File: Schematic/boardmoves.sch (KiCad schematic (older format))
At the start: 27 parts, among them U1 74LS107, U2 74LS107, U3 74LS107, U4 74LS107, U5 74LS107, U6 74LS107, U7 74LS107, U8 74LS107, U9 74LS107

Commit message: More work on the circuit and the PCB layout.
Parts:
- R28, R29, R30, R31, R32, R33, R34, R35, R36: value 10K -> 1K
- U1, U2, U3, U4, U5, U6, U7, U8, U9: value 74LS107 -> 74LS109
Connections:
- wire segments 81 -> 90
- no-connect marks 18 -> 9
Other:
- moved on the sheet: D10, D11, D12, D13, D14, D15, D16, D17, D18, R28, R29, R30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

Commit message: Updated the schematic and PCB with the new flip-flip pinouts and footprints.
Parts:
- U1, U2, U3, U4, U5, U6, U7, U8, U9: footprint Package_DIP:DIP-14_W7.62mm -> Package_DIP:DIP-16_W7.62mm; symbol ttt_ttl-rescue:74LS107 -> local:74LS107
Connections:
- net labels added: Hi
- wire segments 90 -> 108
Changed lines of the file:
@@
 	1200 1600 1300 1600
 NoConn ~ 2600 1350
-Text GLabel 1850 2300 0    60   Input ~ 0
+Text GLabel 1750 850  0    60   Input ~ 0
 Reset
 Wire Wire Line
@@
 	2850 1400 2850 1500
 $Comp
-L ttt_ttl-rescue:74LS107 U2
+L local:74LS107 U2
 U 2 1 5CF796C7
 P 5650 1600
 F 0 "U2" H 5650 1700 50  0000 C CNN
 F 1 "74LS109" H 5650 1500 50  0000 C CNN
-F 2 "Package_DIP:DIP-14_W7.62mm" H 5650 1600 50  0001 C CNN
+F 2 "Package_DIP:DIP-16_W7.62mm" H 5650 1600 50  0001 C CNN
 F 3 "" H 5650 1600 50  0001 C CNN
 	2    5650 1600
@@
 	4900 1600 5000 1600
 NoConn ~ 6300 1350
-Text GLabel 5550 2300 0    60   Input ~ 0
+Text GLabel 5450 850  0    60   Input ~ 0
 Reset
 Wire Wire Line
@@
 	6600 1400 6600 1500
 $Comp
-L ttt_ttl-rescue:74LS107 U3
+L local:74LS107 U3
 U 2 1 5CF79A8E
 P 9200 1600
 F 0 "U3" H 9200 1700 50  0000 C CNN
 F 1 "74LS109" H 9200 1500 50  0000 C CNN
-F 2 "Package_DIP:DIP-14_W7.62mm" H 9200 1600 50  0001 C CNN
+F 2 "Package_DIP:DIP-16_W7.62mm" H 9200 1600 50  0001 C CNN
 F 3 "" H 9200 1600 50  0001 C CNN
 	2    9200 1600
@@
 	8450 1600 8550 1600
 NoConn ~ 9850 1350
-Text GLabel 9100 2300 0    60   Input ~ 0
+Text GLabel 9000 850  0    60   Input ~ 0
 Reset
 Wire Wire Line
@@
 	10050 1400 10050 1500
 $Comp
-L ttt_ttl-rescue:74LS107 U4
+L local:74LS107 U4
 U 2 1 5CF7B138
 P 2000 3650
 F 0 "U4" H 2000 3750 50  0000 C CNN
 F 1 "74LS109" H 2000 3550 50  0000 C CNN
-F 2 "Package_DIP:DIP-14_W7.62mm" H 2000 3650 50  0001 C CNN
+F 2 "Package_DIP:DIP-16_W7.62mm" H 2000 3650 50  0001 C CNN
 F 3 "" H 2000 3650 50  0001 C CNN
 	2    2000 3650
@@
 	1250 3650 1350 3650
 NoConn ~ 2650 3400
-Text GLabel 1900 4350 0    60   Input ~ 0
+Text GLabel 1800 2950 0    60   Input ~ 0
 Reset
 Wire Wire Line
@@
 	2900 3450 2900 3550
 $Comp
-L ttt_ttl-rescue:74LS107 U5
+L local:74LS107 U5
 U 2 1 5CF7B175
 P 5700 3650
 F 0 "U5" H 5700 3750 50  0000 C CNN
 F 1 "74LS109" H 5700 3550 50  0000 C CNN
-F 2 "Package_DIP:DIP-14_W7.62mm" H 5700 3650 50  0001 C CNN
+F 2 "Package_DIP:DIP-16_W7.62mm" H 5700 3650 50  0001 C CNN
 F 3 "" H 5700 3650 50  0001 C CNN
 	2    5700 3650
@@
 	4950 3650 5050 3650
 NoConn ~ 6350 3400
-Text GLabel 5600 4350 0    60   Input ~ 0
+Text GLabel 5550 2900 0    60   Input ~ 0
 Reset
 Wire Wire Line
@@
 	6550 3450 6550 3550
 $Comp
-L ttt_ttl-rescue:74LS107 U6
+L local:74LS107 U6
 U 2 1 5CF7BC48
 P 9250 3650
 F 0 "U6" H 9250 3750 50  0000 C CNN
 F 1 "74LS109" H 9250 3550 50  0000 C CNN
-F 2 "Package_DIP:DIP-14_W7.62mm" H 9250 3650 50  0001 C CNN
+F 2 "Package_DIP:DIP-16_W7.62mm" H 9250 3650 50  0001 C CNN
 F 3 "" H 9250 3650 50  0001 C CNN
 	2    9250 3650
@@
 Wire Wire Line
 	8500 3650 8600 3650
-Text GLabel 9150 4350 0    60   Input ~ 0
+Text GLabel 9050 2900 0    60   Input ~ 0
 Reset
 Wire Wire Line
@@
 	1250 5550 1350 5550
 NoConn ~ 2650 5300
-Text GLabel 1900 6250 0    60   Input ~ 0
+Text GLabel 1850 4800 0    60   Input ~ 0
 Reset
 Wire Wire Line
@@
 Wire Wire Line
 	4950 5550 5050 5550
-Text GLabel 5600 6250 0    60   Input ~ 0
+Text GLabel 5500 4800 0    60   Input ~ 0
 Reset
 Wire Wire Line
 	5600 6250 5700 6250
 $Comp
-L ttt_ttl-rescue:74LS107 U9
+L local:74LS107 U9
 U 2 1 5CF7BC51
 P 9250 5550
 F 0 "U9" H 9250 5650 50  0000 C CNN
 F 1 "74LS109" H 9250 5450 50  0000 C CNN
-F 2 "Package_DIP:DIP-14_W7.62mm" H 9250 5550 50  0001 C CNN
+F 2 "Package_DIP:DIP-16_W7.62mm" H 9250 5550 50  0001 C CNN
 F 3 "" H 9250 5550 50  0001 C CNN
 	2    9250 5550
@@
 Wire Wire Line
 	8500 5550 8600 5550
-Text GLabel 9150 6250 0    60   Input ~ 0
+Text GLabel 9100 4800 0    60   Input ~ 0
 Reset
 Wire Wire Line
@@
 Move8
 $Comp
-L ttt_ttl-rescue:74LS107 U8
+L local:74LS107 U8
 U 2 1 5CF7BC4E
 P 5700 5550
 F 0 "U8" H 5700 5650 50  0000 C CNN
 F 1 "74LS109" H 5700 5450 50  0000 C CNN
-F 2 "Package_DIP:DIP-14_W7.62mm" H 5700 5550 50  0001 C CNN
+F 2 "Package_DIP:DIP-16_W7.62mm" H 5700 5550 50  0001 C CNN
 F 3 "" H 5700 5550 50  0001 C CNN
 	2    5700 5550
@@
 	2650 3900 2900 3900
 $Comp
-L ttt_ttl-rescue:74LS107 U7
+L local:74LS107 U7
 U 2 1 5CF7B867
 P 2000 5550
 F 0 "U7" H 2000 5650 50  0000 C CNN
 F 1 "74LS109" H 2000 5450 50  0000 C CNN
-F 2 "Package_DIP:DIP-14_W7.62mm" H 2000 5550 50  0001 C CNN
+F 2 "Package_DIP:DIP-16_W7.62mm" H 2000 5550 50  0001 C CNN
 F 3 "" H 2000 5550 50  0001 C CNN
 	2    2000 5550
@@
 	1250 5800 1350 5800
 $Comp
-L ttt_ttl-rescue:74LS107 U1
+L local:74LS107 U1
 U 2 1 5CF77C50
 P 1950 1600
 F 0 "U1" H 1950 1700 50  0000 C CNN
 F 1 "74LS109" H 1950 1500 50  0000 C CNN
-F 2 "Package_DIP:DIP-14_W7.62mm" H 1950 1600 50  0001 C CNN
+F 2 "Package_DIP:DIP-16_W7.62mm" H 1950 1600 50  0001 C CNN
 F 3 "" H 1950 1600 50  0001 C CNN
 	2    1950 1600
@@
 Wire Wire Line
 	1200 5300 1350 5300
+Text GLabel 1850 2300 0    50   Input ~ 0
+Hi
+Wire Wire Line
+	1950 1000 1950 850
+Wire Wire Line
+	1950 850  1750 850
+Wire Wire Line
+	5650 1000 5650 850
+Wire Wire Line
+	5650 850  5450 850
+Text GLabel 5550 2300 0    50   Input ~ 0
+Hi
+Wire Wire Line
+	9200 1000 9200 850
+Wire Wire Line
+	9200 850  9000 850
+Text GLabel 9100 2300 0    50   Input ~ 0
+Hi
+Wire Wire Line
+	2000 3050 2000 2950
+Wire Wire Line
+	2000 2950 1800 2950
+Text GLabel 1900 4350 0    50   Input ~ 0
+Hi
+Wire Wire Line
+	5700 3050 5700 2900
+Wire Wire Line
+	5700 2900 5550 2900
+Text GLabel 5600 4350 0    50   Input ~ 0
+Hi
+Wire Wire Line
+	9250 3050 9250 2900
+Wire Wire Line
+	9250 2900 9050 2900
+Text GLabel 9150 4350 0    50   Input ~ 0
+Hi
+Wire Wire Line
+	2000 4950 2000 4800
+Wire Wire Line
+	2000 4800 1850 4800
+Text GLabel 1900 6250 0    50   Input ~ 0
+Hi
+Wire Wire Line
+	5700 4950 5700 4800
+Wire Wire Line
+	5700 4800 5500 4800
+Text GLabel 5600 6250 0    50   Input ~ 0
+Hi
+Wire Wire Line
+	9250 4950 9250 4800
+Wire Wire Line
+	9250 4800 9100 4800
+Text GLabel 9150 6250 0    50   Input ~ 0
+Hi
 $EndSCHEMATC

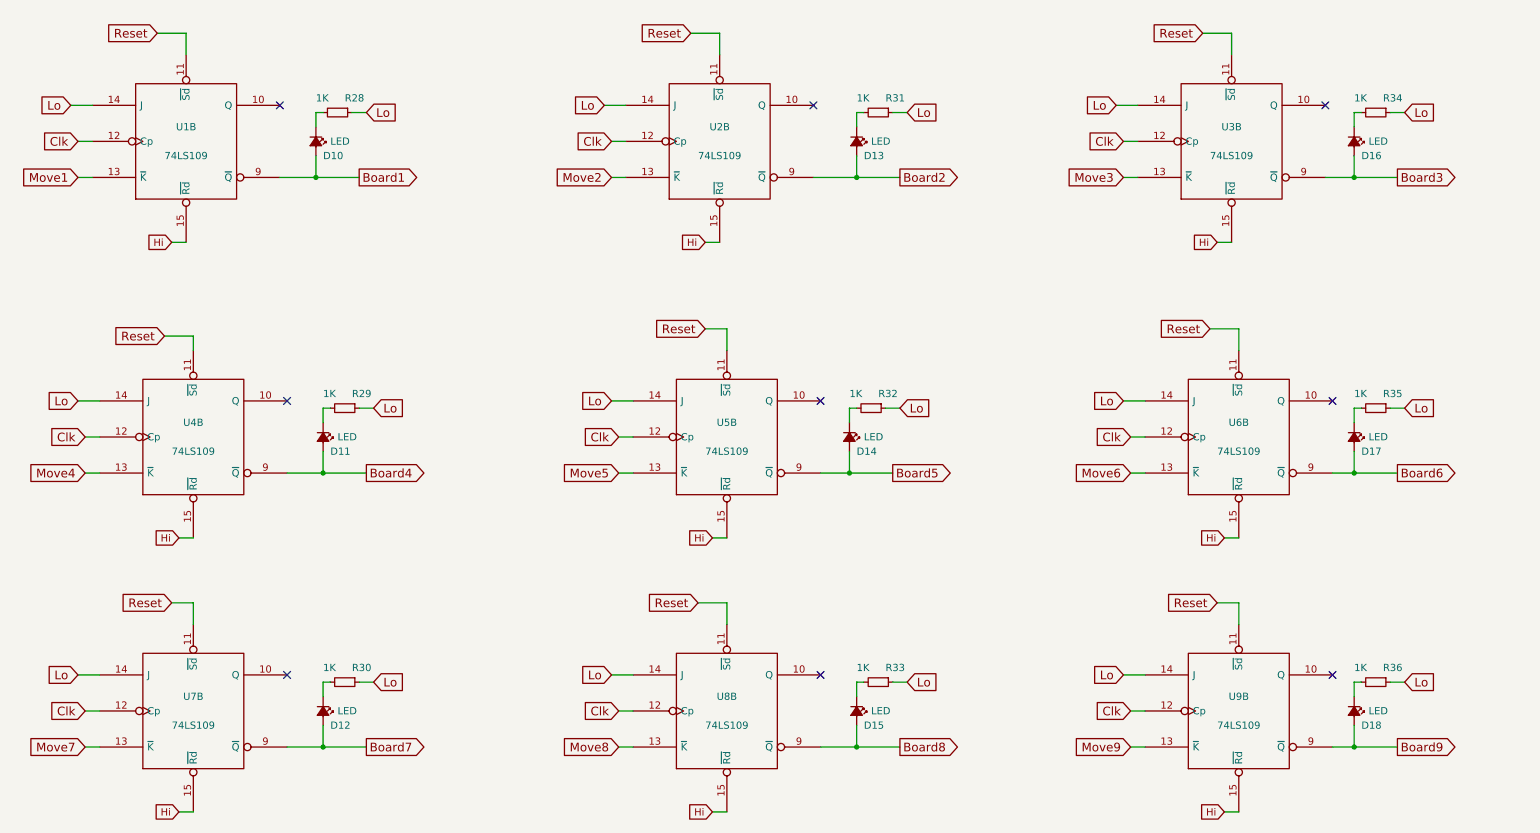
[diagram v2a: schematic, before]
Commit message: Smaller 8Kx8 EEPROM is working
I managed to get the code to generate a ROM file which uses a 4-bit board
state plus the user's moves to look up the net board move and the next
board state. I've redone the schematic, PCB and I've started on the
documentation. I need to redraw the design diagram.
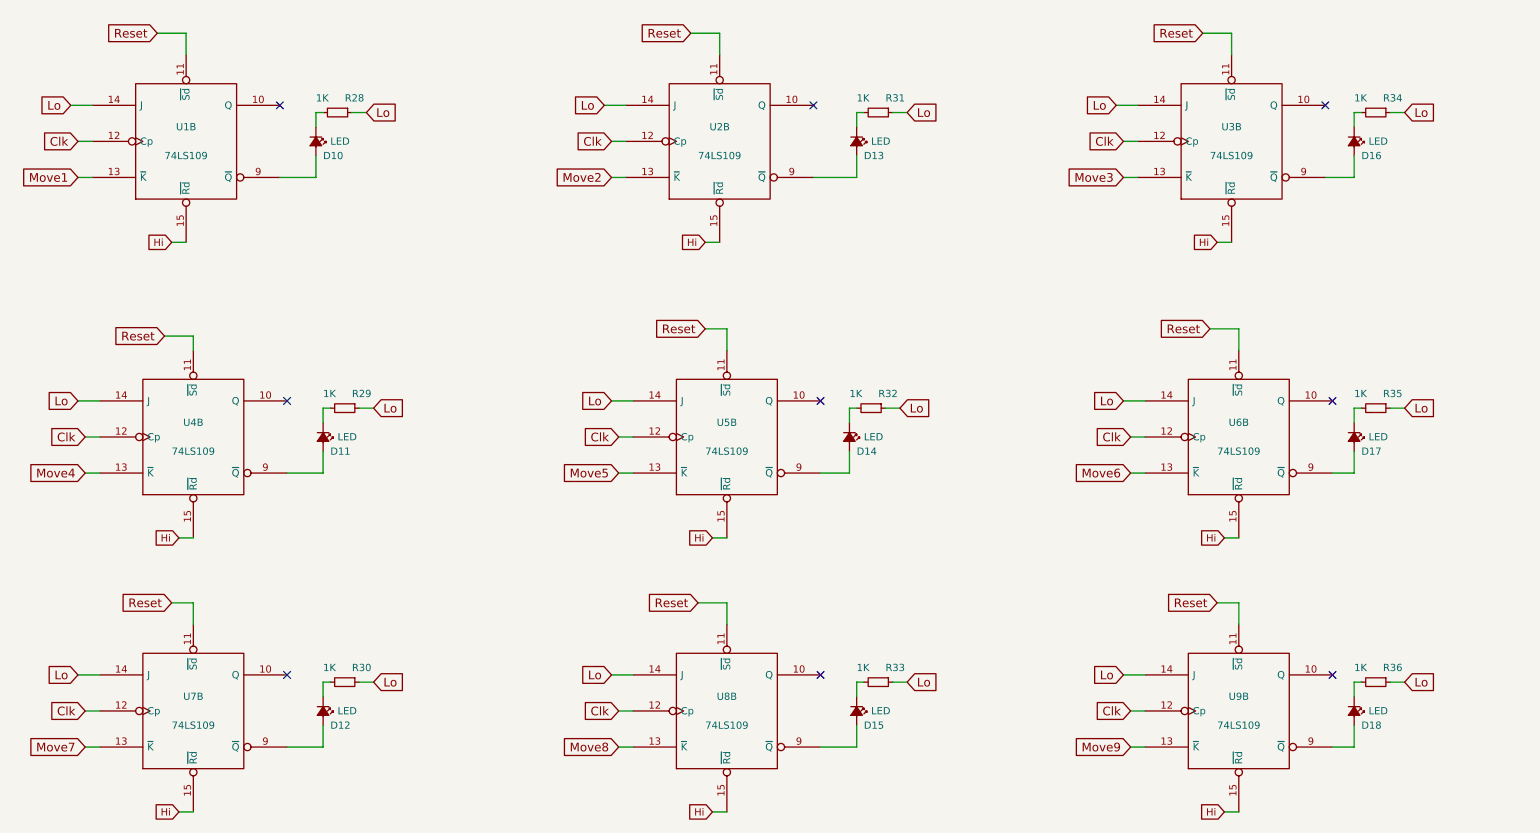
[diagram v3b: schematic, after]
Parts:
- D10, D11, D12, D13, D14, D15, D16, D17, D18: footprint Diode_THT:D_DO-41_SOD81_P7.62mm_Horizontal -> LED_THT:LED_D3.0mm
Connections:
- net Board1: no longer names the net of D10.2 (A), U1.9 (~Q)
- net Board2: no longer names the net of D13.2 (A), U2.9 (~Q)
- net Board3: no longer names the net of D16.2 (A), U3.9 (~Q)
- net Board4: no longer names the net of D11.2 (A), U4.9 (~Q)
- net Board5: no longer names the net of D14.2 (A), U5.9 (~Q)
- net Board6: no longer names the net of D17.2 (A), U6.9 (~Q)
- net Board7: no longer names the net of D12.2 (A), U7.9 (~Q)
- net Board8: no longer names the net of D15.2 (A), U8.9 (~Q)
- net Board9: no longer names the net of D18.2 (A), U9.9 (~Q)
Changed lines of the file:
@@
 Text GLabel 1200 1850 0    60   Input ~ 0
 Move1
-Text GLabel 3150 1850 2    60   Output ~ 0
-Board1
 $Comp
 L ttt_ttl-rescue:LED_Small_ALT D10
@@
 F 0 "D10" V 2950 1650 50  0000 L CNN
 F 1 "LED" V 2850 1700 50  0000 L CNN
-F 2 "Diode_THT:D_DO-41_SOD81_P7.62mm_Horizontal" V 2850 1600 50  0001 C CNN
+F 2 "LED_THT:LED_D3.0mm" V 2850 1600 50  0001 C CNN
 F 3 "" V 2850 1600 50  0001 C CNN
 	1    2850 1600
@@
 Wire Wire Line
 	2850 1700 2850 1850
-Connection ~ 2850 1850
 Wire Wire Line
 	2900 1400 2850 1400
@@
 Text GLabel 4900 1850 0    60   Input ~ 0
 Move2
-Text GLabel 6900 1850 2    60   Output ~ 0
-Board2
 $Comp
 L ttt_ttl-rescue:LED_Small_ALT D13
@@
 F 0 "D13" V 6700 1650 50  0000 L CNN
 F 1 "LED" V 6600 1700 50  0000 L CNN
-F 2 "Diode_THT:D_DO-41_SOD81_P7.62mm_Horizontal" V 6600 1600 50  0001 C CNN
+F 2 "LED_THT:LED_D3.0mm" V 6600 1600 50  0001 C CNN
 F 3 "" V 6600 1600 50  0001 C CNN
 	1    6600 1600
@@
 Wire Wire Line
 	6600 1700 6600 1850
-Connection ~ 6600 1850
 Wire Wire Line
 	6650 1400 6600 1400
@@
 Text GLabel 8450 1850 0    60   Input ~ 0
 Move3
-Text GLabel 10350 1850 2    60   Output ~ 0
-Board3
 $Comp
 L ttt_ttl-rescue:LED_Small_ALT D16
@@
 F 0 "D16" V 10150 1650 50  0000 L CNN
 F 1 "LED" V 10050 1700 50  0000 L CNN
-F 2 "Diode_THT:D_DO-41_SOD81_P7.62mm_Horizontal" V 10050 1600 50  0001 C CNN
+F 2 "LED_THT:LED_D3.0mm" V 10050 1600 50  0001 C CNN
 F 3 "" V 10050 1600 50  0001 C CNN
 	1    10050 1600
@@
 Wire Wire Line
 	10050 1700 10050 1850
-Connection ~ 10050 1850
 Wire Wire Line
 	10100 1400 10050 1400
@@
 Text GLabel 1250 3900 0    60   Input ~ 0
 Move4
-Text GLabel 3200 3900 2    60   Output ~ 0
-Board4
 $Comp
 L ttt_ttl-rescue:LED_Small_ALT D11
@@
 F 0 "D11" V 3000 3700 50  0000 L CNN
 F 1 "LED" V 2900 3750 50  0000 L CNN
-F 2 "Diode_THT:D_DO-41_SOD81_P7.62mm_Horizontal" V 2900 3650 50  0001 C CNN
+F 2 "LED_THT:LED_D3.0mm" V 2900 3650 50  0001 C CNN
 F 3 "" V 2900 3650 50  0001 C CNN
 	1    2900 3650
@@
 Wire Wire Line
 	2900 3750 2900 3900
-Connection ~ 2900 3900
 Wire Wire Line
 	2950 3450 2900 3450
@@
 Text GLabel 4950 3900 0    60   Input ~ 0
 Move5
-Text GLabel 6850 3900 2    60   Output ~ 0
-Board5
 $Comp
 L ttt_ttl-rescue:LED_Small_ALT D14
@@
 F 0 "D14" V 6650 3700 50  0000 L CNN
 F 1 "LED" V 6550 3750 50  0000 L CNN
-F 2 "Diode_THT:D_DO-41_SOD81_P7.62mm_Horizontal" V 6550 3650 50  0001 C CNN
+F 2 "LED_THT:LED_D3.0mm" V 6550 3650 50  0001 C CNN
 F 3 "" V 6550 3650 50  0001 C CNN
 	1    6550 3650
@@
 Wire Wire Line
 	6550 3750 6550 3900
-Connection ~ 6550 3900
 Wire Wire Line
 	6600 3450 6550 3450
@@
 Text GLabel 8500 3900 0    60   Input ~ 0
 Move6
-Text GLabel 10350 3900 2    60   Output ~ 0
-Board6
 $Comp
 L ttt_ttl-rescue:LED_Small_ALT D17
@@
 F 0 "D17" V 10150 3700 50  0000 L CNN
 F 1 "LED" V 10050 3750 50  0000 L CNN
-F 2 "Diode_THT:D_DO-41_SOD81_P7.62mm_Horizontal" V 10050 3650 50  0001 C CNN
+F 2 "LED_THT:LED_D3.0mm" V 10050 3650 50  0001 C CNN
 F 3 "" V 10050 3650 50  0001 C CNN
 	1    10050 3650
@@
 Wire Wire Line
 	10050 3750 10050 3900
-Connection ~ 10050 3900
 Wire Wire Line
 	10100 3450 10050 3450
@@
 Text GLabel 1250 5800 0    60   Input ~ 0
 Move7
-Text GLabel 3200 5800 2    60   Output ~ 0
-Board7
 $Comp
 L ttt_ttl-rescue:LED_Small_ALT D12
@@
 F 0 "D12" V 3000 5600 50  0000 L CNN
 F 1 "LED" V 2900 5650 50  0000 L CNN
-F 2 "Diode_THT:D_DO-41_SOD81_P7.62mm_Horizontal" V 2900 5550 50  0001 C CNN
+F 2 "LED_THT:LED_D3.0mm" V 2900 5550 50  0001 C CNN
 F 3 "" V 2900 5550 50  0001 C CNN
 	1    2900 5550
@@
 Wire Wire Line
 	2900 5650 2900 5800
-Connection ~ 2900 5800
 Wire Wire Line
 	2950 5350 2900 5350
@@
 Text GLabel 8500 5800 0    60   Input ~ 0
 Move9
-Text GLabel 10350 5800 2    60   Output ~ 0
-Board9
 $Comp
 L ttt_ttl-rescue:LED_Small_ALT D18
@@
 F 0 "D18" V 10150 5600 50  0000 L CNN
 F 1 "LED" V 10050 5650 50  0000 L CNN
-F 2 "Diode_THT:D_DO-41_SOD81_P7.62mm_Horizontal" V 10050 5550 50  0001 C CNN
+F 2 "LED_THT:LED_D3.0mm" V 10050 5550 50  0001 C CNN
 F 3 "" V 10050 5550 50  0001 C CNN
 	1    10050 5550
@@
 Wire Wire Line
 	10050 5650 10050 5800
-Connection ~ 10050 5800
 Wire Wire Line
 	10100 5350 10050 5350
 Wire Wire Line
 	10050 5350 10050 5450
-Wire Wire Line
-	2850 1850 3150 1850
-Wire Wire Line
-	6600 1850 6900 1850
-Wire Wire Line
-	10050 1850 10350 1850
-Wire Wire Line
-	2900 3900 3200 3900
-Wire Wire Line
-	6550 3900 6850 3900
-Wire Wire Line
-	10050 3900 10350 3900
-Wire Wire Line
-	2900 5800 3200 5800
-Wire Wire Line
-	10050 5800 10350 5800
 Text GLabel 1250 3650 0    60   Input ~ 0
 Clk
@@
 	4950 5800 5050 5800
 Wire Wire Line
-	6600 5800 6900 5800
-Wire Wire Line
 	6600 5350 6600 5450
 Wire Wire Line
 	6650 5350 6600 5350
-Connection ~ 6600 5800
 Wire Wire Line
 	6600 5650 6600 5800
@@
 F 0 "D15" V 6700 5600 50  0000 L CNN
 F 1 "LED" V 6600 5650 50  0000 L CNN
-F 2 "Diode_THT:D_DO-41_SOD81_P7.62mm_Horizontal" V 6600 5550 50  0001 C CNN
+F 2 "LED_THT:LED_D3.0mm" V 6600 5550 50  0001 C CNN
 F 3 "" V 6600 5550 50  0001 C CNN
 	1    6600 5550
 	0    1    1    0
 $EndComp
-Text GLabel 6900 5800 2    60   Output ~ 0
-Board8
 Wire Wire Line
 	6350 5800 6600 5800

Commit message: Changed to horizontal resistors on PCB.
This resulted in only two vias, so that's nice.
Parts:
- R28, R29, R30, R31, R32, R33, R34, R35, R36: footprint Resistor_THT:R_Axial_DIN0204_L3.6mm_D1.6mm_P1.90mm_Vertical -> Resistor_THT:R_Axial_DIN0207_L6.3mm_D2.5mm_P7.62mm_Horizontal
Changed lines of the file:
@@
 F 0 "R28" V 2900 1450 50  0000 L CNN
 F 1 "1K" V 2900 1250 50  0000 L CNN
-F 2 "Resistor_THT:R_Axial_DIN0204_L3.6mm_D1.6mm_P1.90mm_Vertical" H 3000 1400 50  0001 C CNN
+F 2 "Resistor_THT:R_Axial_DIN0207_L6.3mm_D2.5mm_P7.62mm_Horizontal" H 3000 1400 50  0001 C CNN
 F 3 "" H 3000 1400 50  0001 C CNN
 	1    3000 1400
@@
 F 0 "R31" V 6650 1450 50  0000 L CNN
 F 1 "1K" V 6650 1250 50  0000 L CNN
-F 2 "Resistor_THT:R_Axial_DIN0204_L3.6mm_D1.6mm_P1.90mm_Vertical" H 6750 1400 50  0001 C CNN
+F 2 "Resistor_THT:R_Axial_DIN0207_L6.3mm_D2.5mm_P7.62mm_Horizontal" H 6750 1400 50  0001 C CNN
 F 3 "" H 6750 1400 50  0001 C CNN
 	1    6750 1400
@@
 F 0 "R34" V 10100 1450 50  0000 L CNN
 F 1 "1K" V 10100 1250 50  0000 L CNN
-F 2 "Resistor_THT:R_Axial_DIN0204_L3.6mm_D1.6mm_P1.90mm_Vertical" H 10200 1400 50  0001 C CNN
+F 2 "Resistor_THT:R_Axial_DIN0207_L6.3mm_D2.5mm_P7.62mm_Horizontal" H 10200 1400 50  0001 C CNN
 F 3 "" H 10200 1400 50  0001 C CNN
 	1    10200 1400
@@
 F 0 "R29" V 2950 3500 50  0000 L CNN
 F 1 "1K" V 2950 3300 50  0000 L CNN
-F 2 "Resistor_THT:R_Axial_DIN0204_L3.6mm_D1.6mm_P1.90mm_Vertical" H 3050 3450 50  0001 C CNN
+F 2 "Resistor_THT:R_Axial_DIN0207_L6.3mm_D2.5mm_P7.62mm_Horizontal" H 3050 3450 50  0001 C CNN
 F 3 "" H 3050 3450 50  0001 C CNN
 	1    3050 3450
@@
 F 0 "R32" V 6600 3500 50  0000 L CNN
 F 1 "1K" V 6600 3300 50  0000 L CNN
-F 2 "Resistor_THT:R_Axial_DIN0204_L3.6mm_D1.6mm_P1.90mm_Vertical" H 6700 3450 50  0001 C CNN
+F 2 "Resistor_THT:R_Axial_DIN0207_L6.3mm_D2.5mm_P7.62mm_Horizontal" H 6700 3450 50  0001 C CNN
 F 3 "" H 6700 3450 50  0001 C CNN
 	1    6700 3450
@@
 F 0 "R35" V 10100 3500 50  0000 L CNN
 F 1 "1K" V 10100 3300 50  0000 L CNN
-F 2 "Resistor_THT:R_Axial_DIN0204_L3.6mm_D1.6mm_P1.90mm_Vertical" H 10200 3450 50  0001 C CNN
+F 2 "Resistor_THT:R_Axial_DIN0207_L6.3mm_D2.5mm_P7.62mm_Horizontal" H 10200 3450 50  0001 C CNN
 F 3 "" H 10200 3450 50  0001 C CNN
 	1    10200 3450
@@
 F 0 "R30" V 2950 5400 50  0000 L CNN
 F 1 "1K" V 2950 5200 50  0000 L CNN
-F 2 "Resistor_THT:R_Axial_DIN0204_L3.6mm_D1.6mm_P1.90mm_Vertical" H 3050 5350 50  0001 C CNN
+F 2 "Resistor_THT:R_Axial_DIN0207_L6.3mm_D2.5mm_P7.62mm_Horizontal" H 3050 5350 50  0001 C CNN
 F 3 "" H 3050 5350 50  0001 C CNN
 	1    3050 5350
@@
 F 0 "R36" V 10100 5400 50  0000 L CNN
 F 1 "1K" V 10100 5200 50  0000 L CNN
-F 2 "Resistor_THT:R_Axial_DIN0204_L3.6mm_D1.6mm_P1.90mm_Vertical" H 10200 5350 50  0001 C CNN
+F 2 "Resistor_THT:R_Axial_DIN0207_L6.3mm_D2.5mm_P7.62mm_Horizontal" H 10200 5350 50  0001 C CNN
 F 3 "" H 10200 5350 50  0001 C CNN
 	1    10200 5350
@@
 F 0 "R33" V 6650 5400 50  0000 L CNN
 F 1 "1K" V 6650 5200 50  0000 L CNN
-F 2 "Resistor_THT:R_Axial_DIN0204_L3.6mm_D1.6mm_P1.90mm_Vertical" H 6750 5350 50  0001 C CNN
+F 2 "Resistor_THT:R_Axial_DIN0207_L6.3mm_D2.5mm_P7.62mm_Horizontal" H 6750 5350 50  0001 C CNN
 F 3 "" H 6750 5350 50  0001 C CNN
 	1    6750 5350
